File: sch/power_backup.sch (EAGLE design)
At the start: 34 parts, among them IC1 78L05SMD, IC2 ACS712-LC, K1 DS2Y-S-DC48V, T1 BC847, T2 BC847, T3 BC847

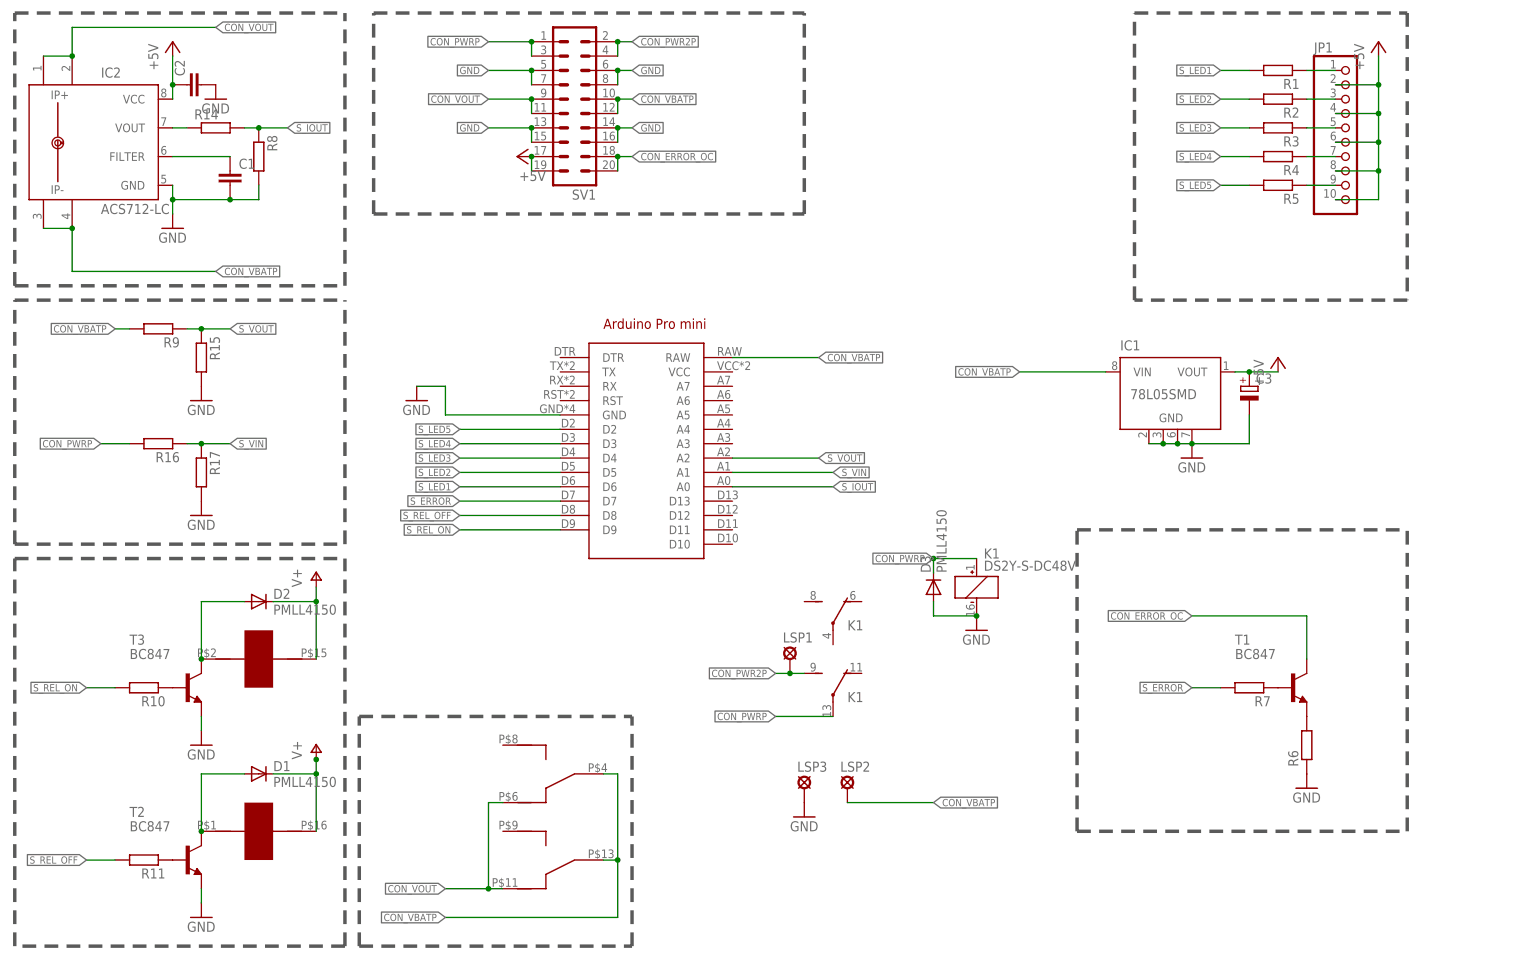
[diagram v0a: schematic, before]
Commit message: Enclosure image and schematic added
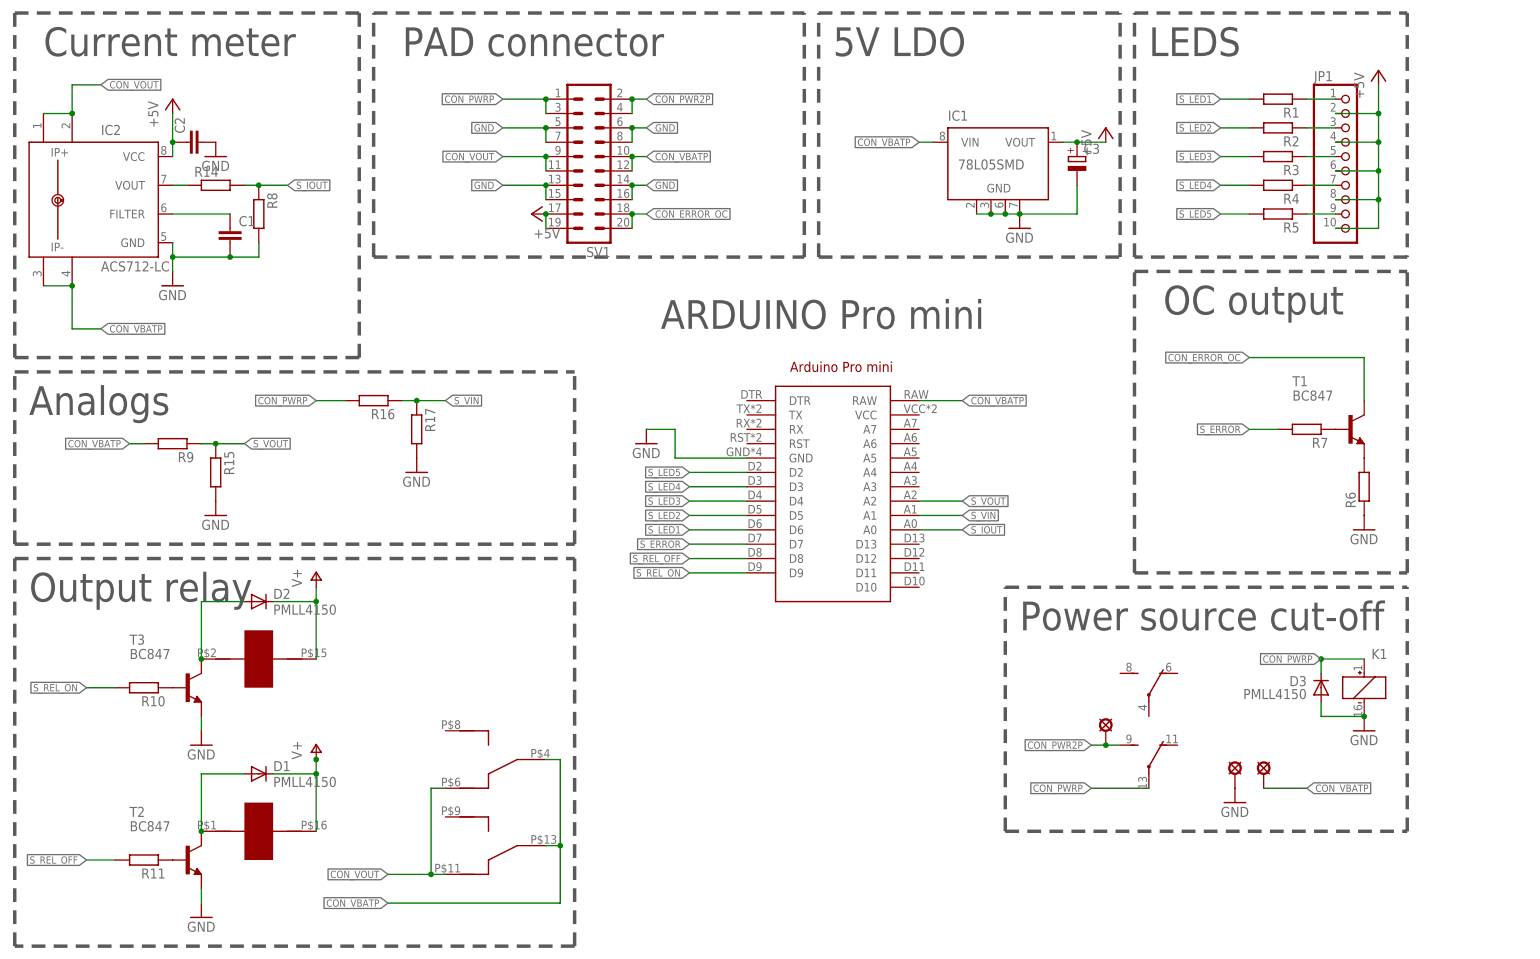
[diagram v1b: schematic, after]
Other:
- note added: "5V LDO"
- note added: "ARDUINO Pro mini"
- note added: "Analogs"
- note added: "Current meter"
- note added: "LEDS"
- note added: "OC output"
- note added: "Output relay"
- note added: "PAD connector"
- note added: "Power source cut-off"
- note added: "We ignore VCC-5V from arduino assume that it can be 3V"
- moved on the sheet: C1, C2, C3, D3, IC1, IC2, JP1, K1, R1, R14, R15, R16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
